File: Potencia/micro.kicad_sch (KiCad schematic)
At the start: 14 parts, among them J2 Relay, Q1 PN2222A, Q2 PN2222A

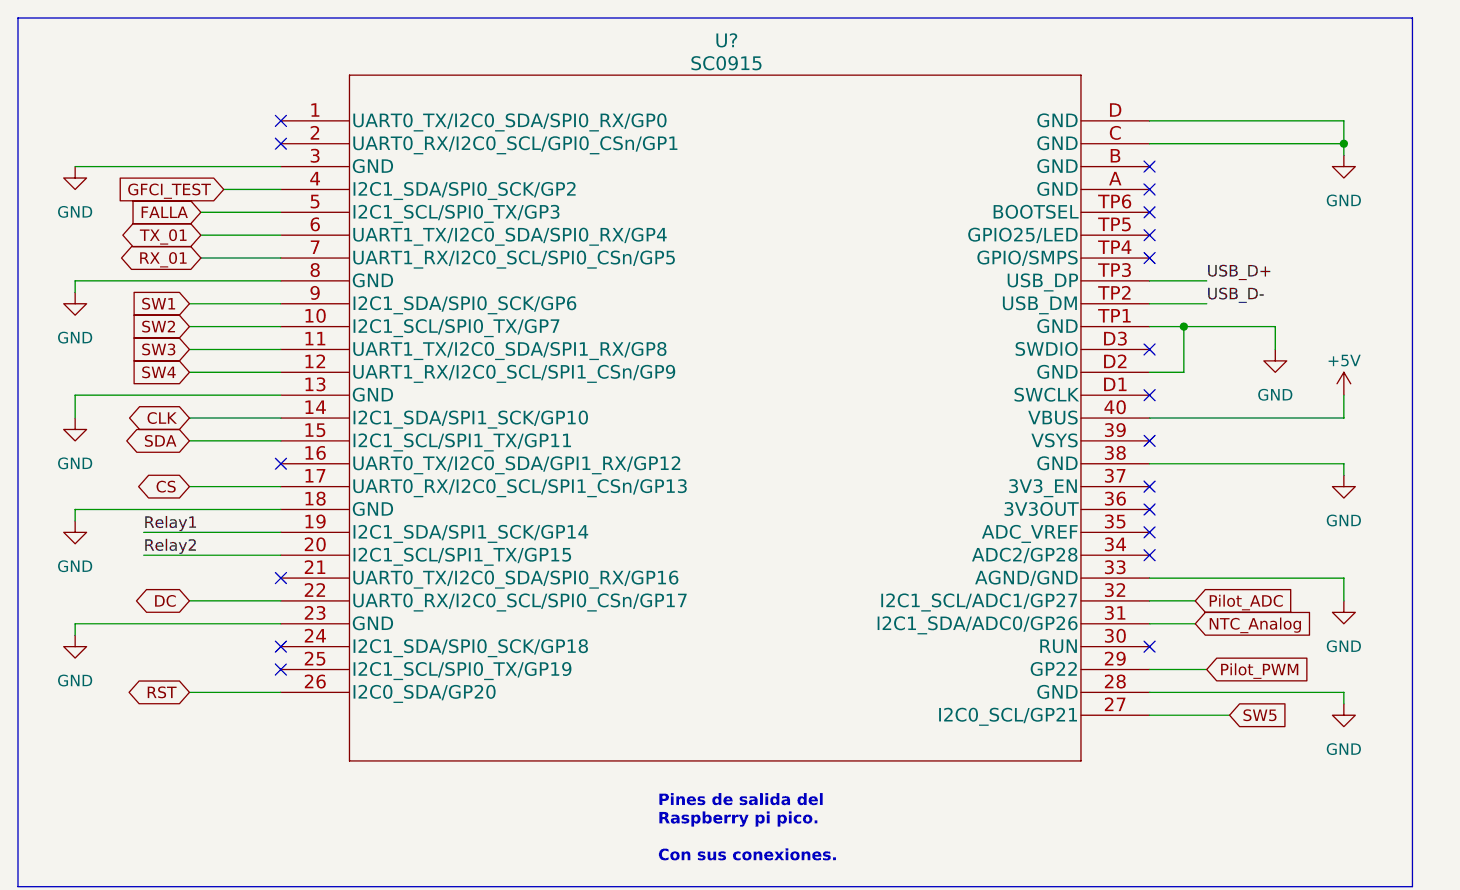
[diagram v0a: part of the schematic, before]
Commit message: Se modifica la ubicación de pines
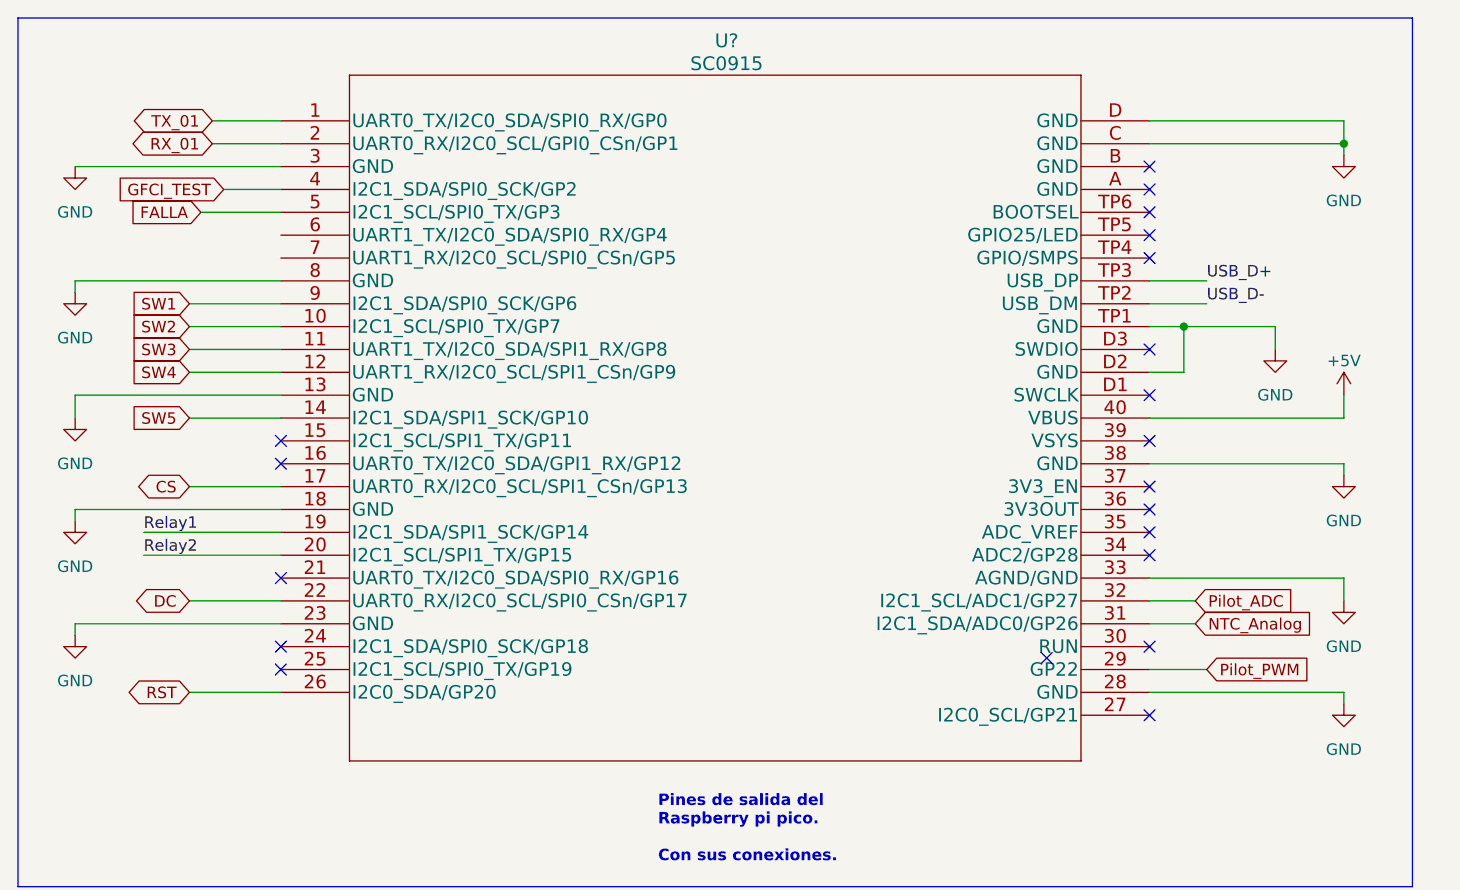
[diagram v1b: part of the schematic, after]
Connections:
- net CLK: no longer U?.14 (I2C1_SDA/SPI1_SCK/GP10)
- net RX_01: now also U?.2 (UART0_RX/I2C0_SCL/GPI0_CSn/GP1); no longer U?.7 (UART1_RX/I2C0_SCL/SPI0_CSn/GP5)
- net SDA: no longer U?.15 (I2C1_SCL/SPI1_TX/GP11)
- net SW5: now also U?.14 (I2C1_SDA/SPI1_SCK/GP10); no longer U?.27 (I2C0_SCL/GP21)
- net TX_01: now also U?.1 (UART0_TX/I2C0_SDA/SPI0_RX/GP0); no longer U?.6 (UART1_TX/I2C0_SDA/SPI0_RX/GP4)
- no-connect marks 19 -> 20
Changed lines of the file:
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@@
   )
   (no_connect (at 46.99 85.09))
+  (no_connect (at 46.99 62.23))
   (no_connect (at 46.99 87.63))
   (no_connect (at 143.51 67.31))
   (no_connect (at 143.51 41.91))
   (no_connect (at 143.51 34.29))
+  (no_connect (at 143.51 92.71))
   (no_connect (at 143.51 39.37))
+  (no_connect (at 132.08 86.36))
   (no_connect (at 143.51 85.09))
   (no_connect (at 143.51 62.23))
   (no_connect (at 143.51 69.85))
-  (no_connect (at 46.99 29.21))
   (no_connect (at 143.51 31.75))
-  (no_connect (at 46.99 26.67))
   (no_connect (at 143.51 57.15))
   (no_connect (at 143.51 72.39))
@@
     (stroke (width 0) (type default))
   )
-  (wire (pts (xy 143.51 92.71) (xy 152.4 92.71))
-    (stroke (width 0) (type default))
-  )
   (wire (pts (xy 233.68 66.04) (xy 240.03 66.04))
     (stroke (width 0) (type default))
@@
     (stroke (width 0) (type default))
   )
+  (wire (pts (xy 39.37 26.67) (xy 46.99 26.67))
+    (stroke (width 0) (type default))
+  )
   (wire (pts (xy 143.51 44.45) (xy 149.86 44.45))
     (stroke (width 0) (type default))
@@
     (stroke (width 0) (type default))
   )
+  (wire (pts (xy 36.83 59.69) (xy 46.99 59.69))
+    (stroke (width 0) (type default))
+  )
   (wire (pts (xy 147.32 49.53) (xy 147.32 54.61))
     (stroke (width 0) (type default))
@@
     (stroke (width 0) (type default))
   )
-  (wire (pts (xy 38.1 41.91) (xy 46.99 41.91))
-    (stroke (width 0) (type default))
-  )
   (wire (pts (xy 45.72 152.4) (xy 48.26 152.4))
     (stroke (width 0) (type default))
@@
     (stroke (width 0) (type default))
   )
+  (wire (pts (xy 39.37 29.21) (xy 46.99 29.21))
+    (stroke (width 0) (type default))
+  )
   (wire (pts (xy 36.83 90.17) (xy 46.99 90.17))
     (stroke (width 0) (type default))
@@
     (stroke (width 0) (type default))
   )
-  (wire (pts (xy 36.83 62.23) (xy 46.99 62.23))
-    (stroke (width 0) (type default))
-  )
   (wire (pts (xy 124.46 138.43) (xy 124.46 139.7))
     (stroke (width 0) (type default))
@@
     (stroke (width 0) (type default))
   )
-  (wire (pts (xy 36.83 59.69) (xy 46.99 59.69))
-    (stroke (width 0) (type default))
-  )
   (wire (pts (xy 45.72 161.29) (xy 48.26 161.29))
     (stroke (width 0) (type default))
@@
   )
   (wire (pts (xy 165.1 30.48) (xy 165.1 29.21))
-    (stroke (width 0) (type default))
-  )
-  (wire (pts (xy 38.1 39.37) (xy 46.99 39.37))
     (stroke (width 0) (type default))
   )
@@
     )
   )
-  (global_label "SDA" (shape bidirectional) (at 36.83 62.23 180) (fields_autoplaced)
-    (effects (font (size 1.27 1.27)) (justify right))
-    (property "Intersheetrefs" "${INTERSHEET_REFS}" (at 29.2448 62.23 0)
-      (effects (font (size 1.27 1.27)) (justify right) hide)
-    )
-  )
-  (global_label "TX_01" (shape bidirectional) (at 38.1 39.37 180) (fields_autoplaced)
-    (effects (font (size 1.27 1.27)) (justify right))
-    (property "Intersheetrefs" "${INTERSHEET_REFS}" (at 28.5192 39.37 0)
+  (global_label "TX_01" (shape bidirectional) (at 39.37 26.67 180) (fields_autoplaced)
+    (effects (font (size 1.27 1.27)) (justify right))
+    (property "Intersheetrefs" "${INTERSHEET_REFS}" (at 29.7892 26.67 0)
       (effects (font (size 1.27 1.27)) (justify right) hide)
     )
@@
     )
   )
-  (global_label "RX_01" (shape bidirectional) (at 38.1 41.91 180) (fields_autoplaced)
-    (effects (font (size 1.27 1.27)) (justify right))
-    (property "Intersheetrefs" "${INTERSHEET_REFS}" (at 28.2168 41.91 0)
+  (global_label "RX_01" (shape bidirectional) (at 39.37 29.21 180) (fields_autoplaced)
+    (effects (font (size 1.27 1.27)) (justify right))
+    (property "Intersheetrefs" "${INTERSHEET_REFS}" (at 29.4868 29.21 0)
       (effects (font (size 1.27 1.27)) (justify right) hide)
     )
@@
     )
   )
-  (global_label "CLK" (shape bidirectional) (at 36.83 59.69 180) (fields_autoplaced)
-    (effects (font (size 1.27 1.27)) (justify right))
-    (property "Intersheetrefs" "${INTERSHEET_REFS}" (at 29.2448 59.69 0)
-      (effects (font (size 1.27 1.27)) (justify right) hide)
-    )
-  )
   (global_label "DC" (shape bidirectional) (at 119.38 156.21 0) (fields_autoplaced)
     (effects (font (size 1.27 1.27)) (justify left))
@@
     )
   )
-  (global_label "SW5" (shape input) (at 152.4 92.71 0) (fields_autoplaced)
-    (effects (font (size 1.27 1.27)) (justify left))
-    (property "Intersheetrefs" "${INTERSHEET_REFS}" (at 159.1762 92.71 0)
-      (effects (font (size 1.27 1.27)) (justify left) hide)
-    )
-  )
+  (global_label "SW5" (shape input) (at 36.83 59.69 180) (fields_autoplaced)
+    (effects (font (size 1.27 1.27)) (justify right))
+    (property "Intersheetrefs" "${INTERSHEET_REFS}" (at 30.0538 59.69 0)
+      (effects (font (size 1.27 1.27)) (justify right) hide)
+    )
+  )

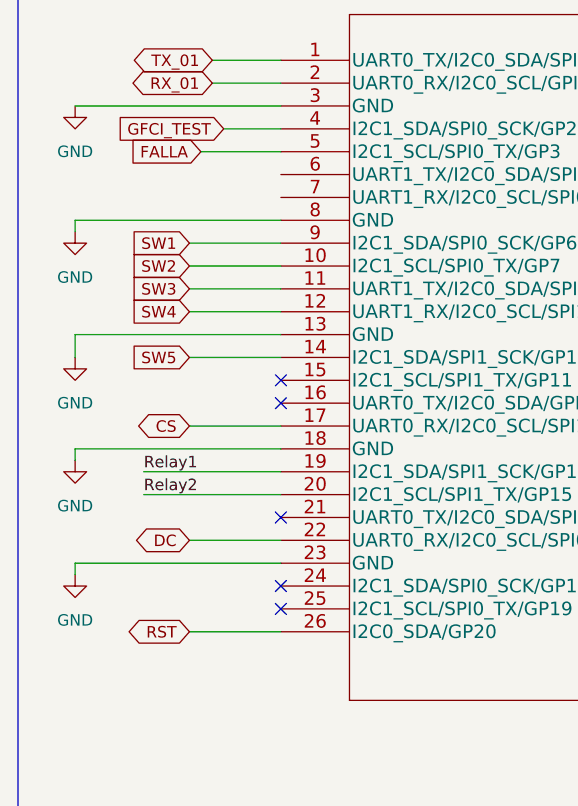
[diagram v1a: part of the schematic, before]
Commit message: Cambio de pantalla
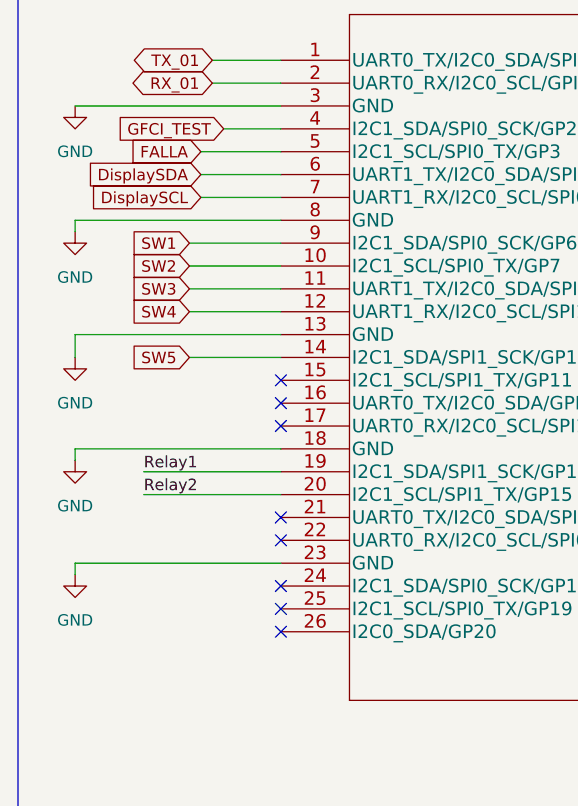
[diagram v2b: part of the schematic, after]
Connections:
- net CS: no longer U?.17 (UART0_RX/I2C0_SCL/SPI1_CSn/GP13)
- net DC: no longer U?.22 (UART0_RX/I2C0_SCL/SPI0_CSn/GP17)
- net RST: no longer U?.26 (I2C0_SDA/GP20)
- net DisplaySDA: now reaches U?.6 (UART1_TX/I2C0_SDA/SPI0_RX/GP4)
- net DisplaySCL: now reaches U?.7 (UART1_RX/I2C0_SCL/SPI0_CSn/GP5)
- no-connect marks 20 -> 23
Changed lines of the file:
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@@
   (no_connect (at 143.51 52.07))
   (no_connect (at 143.51 74.93))
+  (no_connect (at 46.99 67.31))
+  (no_connect (at 46.99 90.17))
   (no_connect (at 143.51 36.83))
   (no_connect (at 46.99 77.47))
   (no_connect (at 46.99 64.77))
+  (no_connect (at 46.99 80.01))
   (wire (pts (xy 233.68 33.02) (xy 240.03 33.02))
     (stroke (width 0) (type default))
   )
-  (wire (pts (xy 36.83 80.01) (xy 46.99 80.01))
+  (wire (pts (xy 38.1 39.37) (xy 46.99 39.37))
     (stroke (width 0) (type default))
   )
@@
     (stroke (width 0) (type default))
   )
-  (wire (pts (xy 36.83 67.31) (xy 46.99 67.31))
-    (stroke (width 0) (type default))
-  )
   (wire (pts (xy 143.51 64.77) (xy 165.1 64.77))
     (stroke (width 0) (type default))
@@
     (stroke (width 0) (type default))
   )
-  (wire (pts (xy 36.83 90.17) (xy 46.99 90.17))
-    (stroke (width 0) (type default))
-  )
   (wire (pts (xy 247.65 38.1) (xy 247.65 39.37))
     (stroke (width 0) (type default))
@@
   )
   (wire (pts (xy 222.25 33.02) (xy 226.06 33.02))
+    (stroke (width 0) (type default))
+  )
+  (wire (pts (xy 38.1 41.91) (xy 46.99 41.91))
     (stroke (width 0) (type default))
   )
@@
     )
   )
-  (global_label "CS" (shape bidirectional) (at 36.83 67.31 180) (fields_autoplaced)
-    (effects (font (size 1.27 1.27)) (justify right))
-    (property "Intersheetrefs" "${INTERSHEET_REFS}" (at 30.3334 67.31 0)
-      (effects (font (size 1.27 1.27)) (justify right) hide)
-    )
-  )
   (global_label "SW4" (shape input) (at 36.83 54.61 180) (fields_autoplaced)
     (effects (font (size 1.27 1.27)) (justify right))
@@
     )
   )
+  (global_label "DisplaySDA" (shape input) (at 38.1 39.37 180) (fields_autoplaced)
+    (effects (font (size 1.27 1.27)) (justify right))
+    (property "Intersheetrefs" "${INTERSHEET_REFS}" (at 24.7924 39.37 0)
+      (effects (font (size 1.27 1.27)) (justify right) hide)
+    )
+  )
   (global_label "SW3" (shape input) (at 36.83 52.07 180) (fields_autoplaced)
     (effects (font (size 1.27 1.27)) (justify right))
@@
     )
   )
-  (global_label "DC" (shape bidirectional) (at 36.83 80.01 180) (fields_autoplaced)
-    (effects (font (size 1.27 1.27)) (justify right))
-    (property "Intersheetrefs" "${INTERSHEET_REFS}" (at 30.2729 80.01 0)
+  (global_label "DisplaySCL" (shape input) (at 38.1 41.91 180) (fields_autoplaced)
+    (effects (font (size 1.27 1.27)) (justify right))
+    (property "Intersheetrefs" "${INTERSHEET_REFS}" (at 24.8529 41.91 0)
       (effects (font (size 1.27 1.27)) (justify right) hide)
     )
@@
     )
   )
-  (global_label "RST" (shape bidirectional) (at 36.83 90.17 180) (fields_autoplaced)
-    (effects (font (size 1.27 1.27)) (justify right))
-    (property "Intersheetrefs" "${INTERSHEET_REFS}" (at 29.3658 90.17 0)
-      (effects (font (size 1.27 1.27)) (justify right) hide)
-    )
-  )
